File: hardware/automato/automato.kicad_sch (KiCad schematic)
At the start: 86 parts, among them J1 Motor1, J10 Servo 3, J11 Servo 4, J12 Barrel_Jack, J2 Motor2, J3 Motor4, J4 Motor3, J5 Servo 1, J6 i2c, J7 Servo 2, J8 Relay 1, J9 Relay 2, K1 G5Q-1A, K2 G5Q-1A, Q1 AO3400A, Q2 AO3400A, Q3 AO3400A, Q4 AO3400A, Q5 AO3400A, Q6 AO3400A, Q7 HY12P03C2, U1 ESP32-C6-DEVKITC-1-N8, U6 TPS5450DDAR

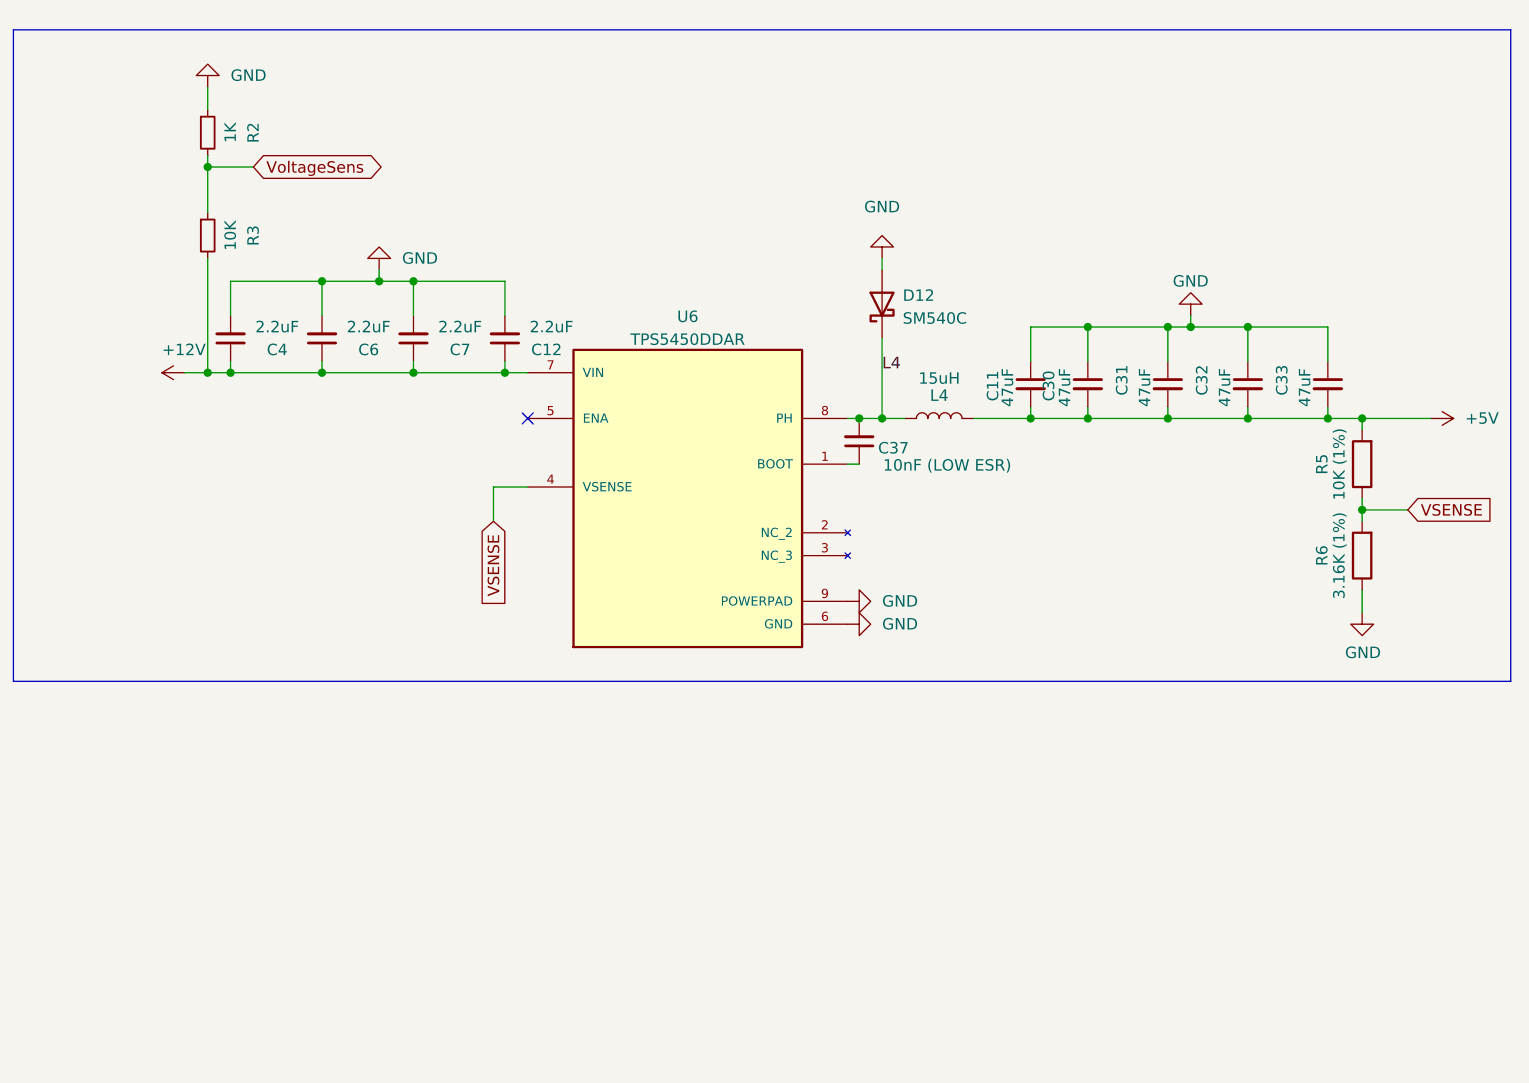
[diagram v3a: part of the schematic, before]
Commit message: added growlight
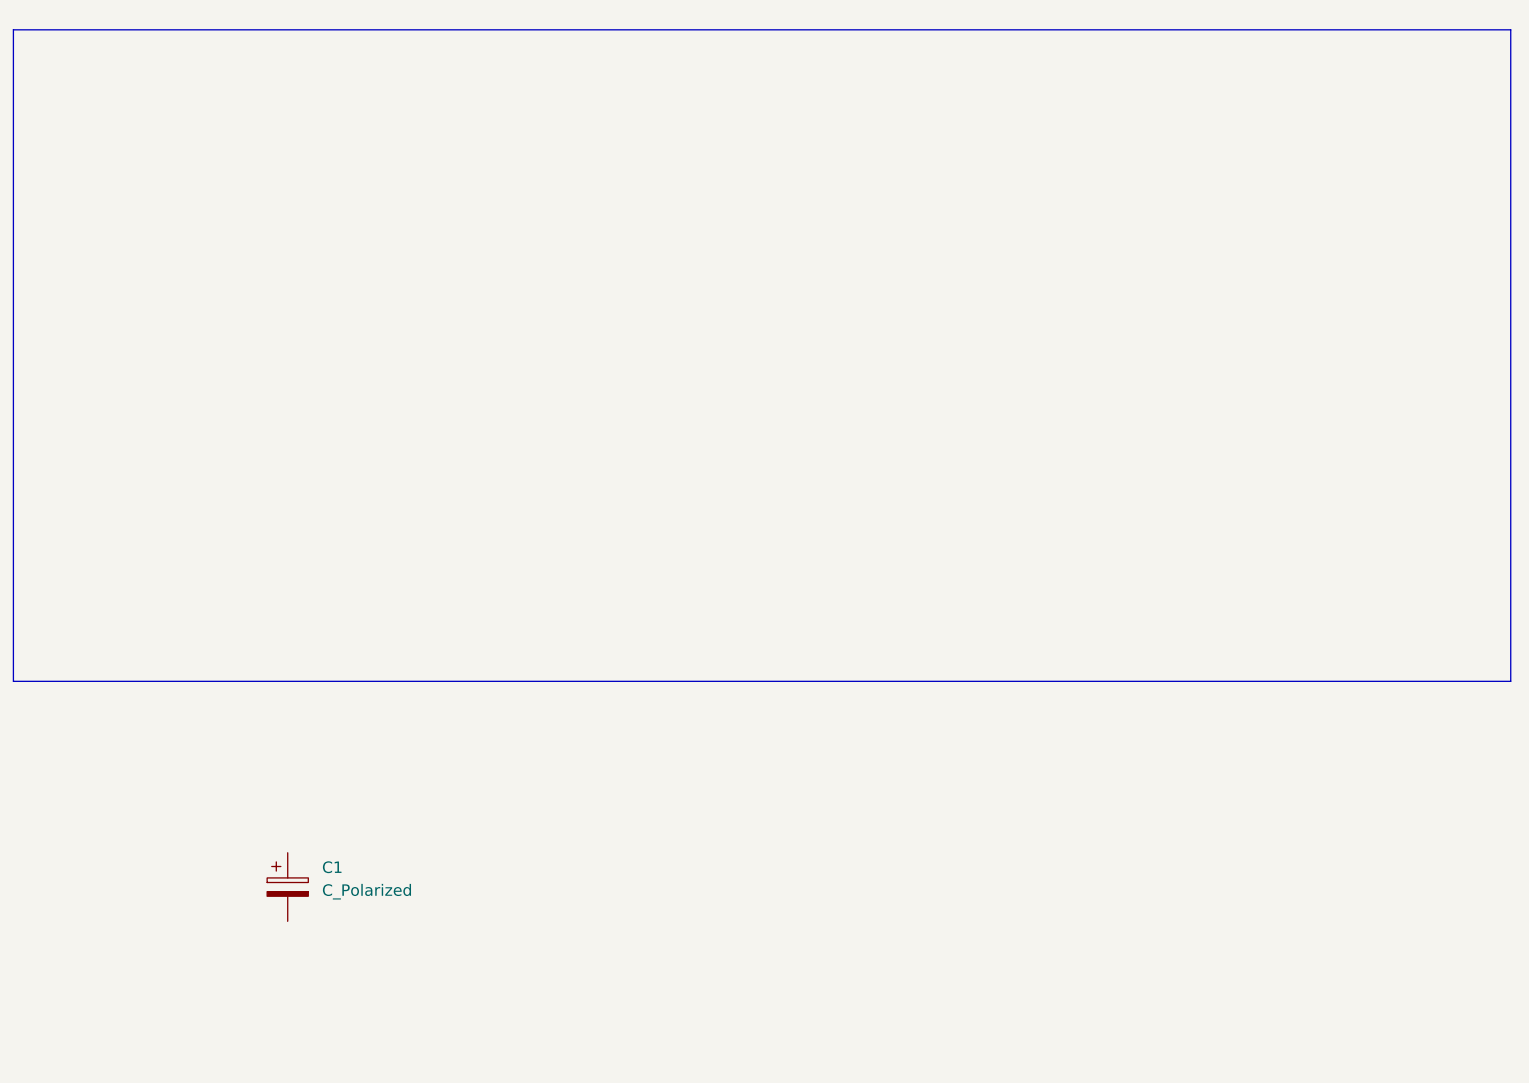
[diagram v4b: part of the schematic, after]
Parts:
- removed C11, C30, C31, C32, C33: 47uF, Capacitor_SMD:C_0805_2012Metric, symbol Device:C_Small
- removed C12, C4, C6, C7: 2.2uF, Capacitor_SMD:C_0805_2012Metric, symbol Device:C_Small
- removed C37: 10nF (LOW ESR), Capacitor_SMD:C_0402_1005Metric, symbol Device:C_Small
- removed D12: SM540C, Diode_SMD:D_SMC, symbol Device:D_Schottky
- removed L4: 15uH, BlackPanda:L_10.5x11.5_H4.0, symbol Device:L
- removed R2: 1K, Resistor_SMD:R_0402_1005Metric, symbol Device:R_Small
- removed R3: 10K, Resistor_SMD:R_0402_1005Metric, symbol Device:R_Small
- removed R5: 10K (1%), Resistor_SMD:R_0402_1005Metric, symbol Device:R
- removed R6: 3.16K (1%), Capacitor_SMD:C_0603_1608Metric, symbol Device:R
- removed U6: TPS5450DDAR, BlackPanda:CONV_TPS5450DDAR, symbol TPS5450DDAR:TPS5450DDAR
- added C1: C_Polarized, symbol Device:C_Polarized
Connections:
- no-connect marks 10 -> 9
